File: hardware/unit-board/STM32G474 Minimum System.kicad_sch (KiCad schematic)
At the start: 19 parts, among them U4 STM32G474RET6, Y1 ECS-80-8-33Q-JES-TR

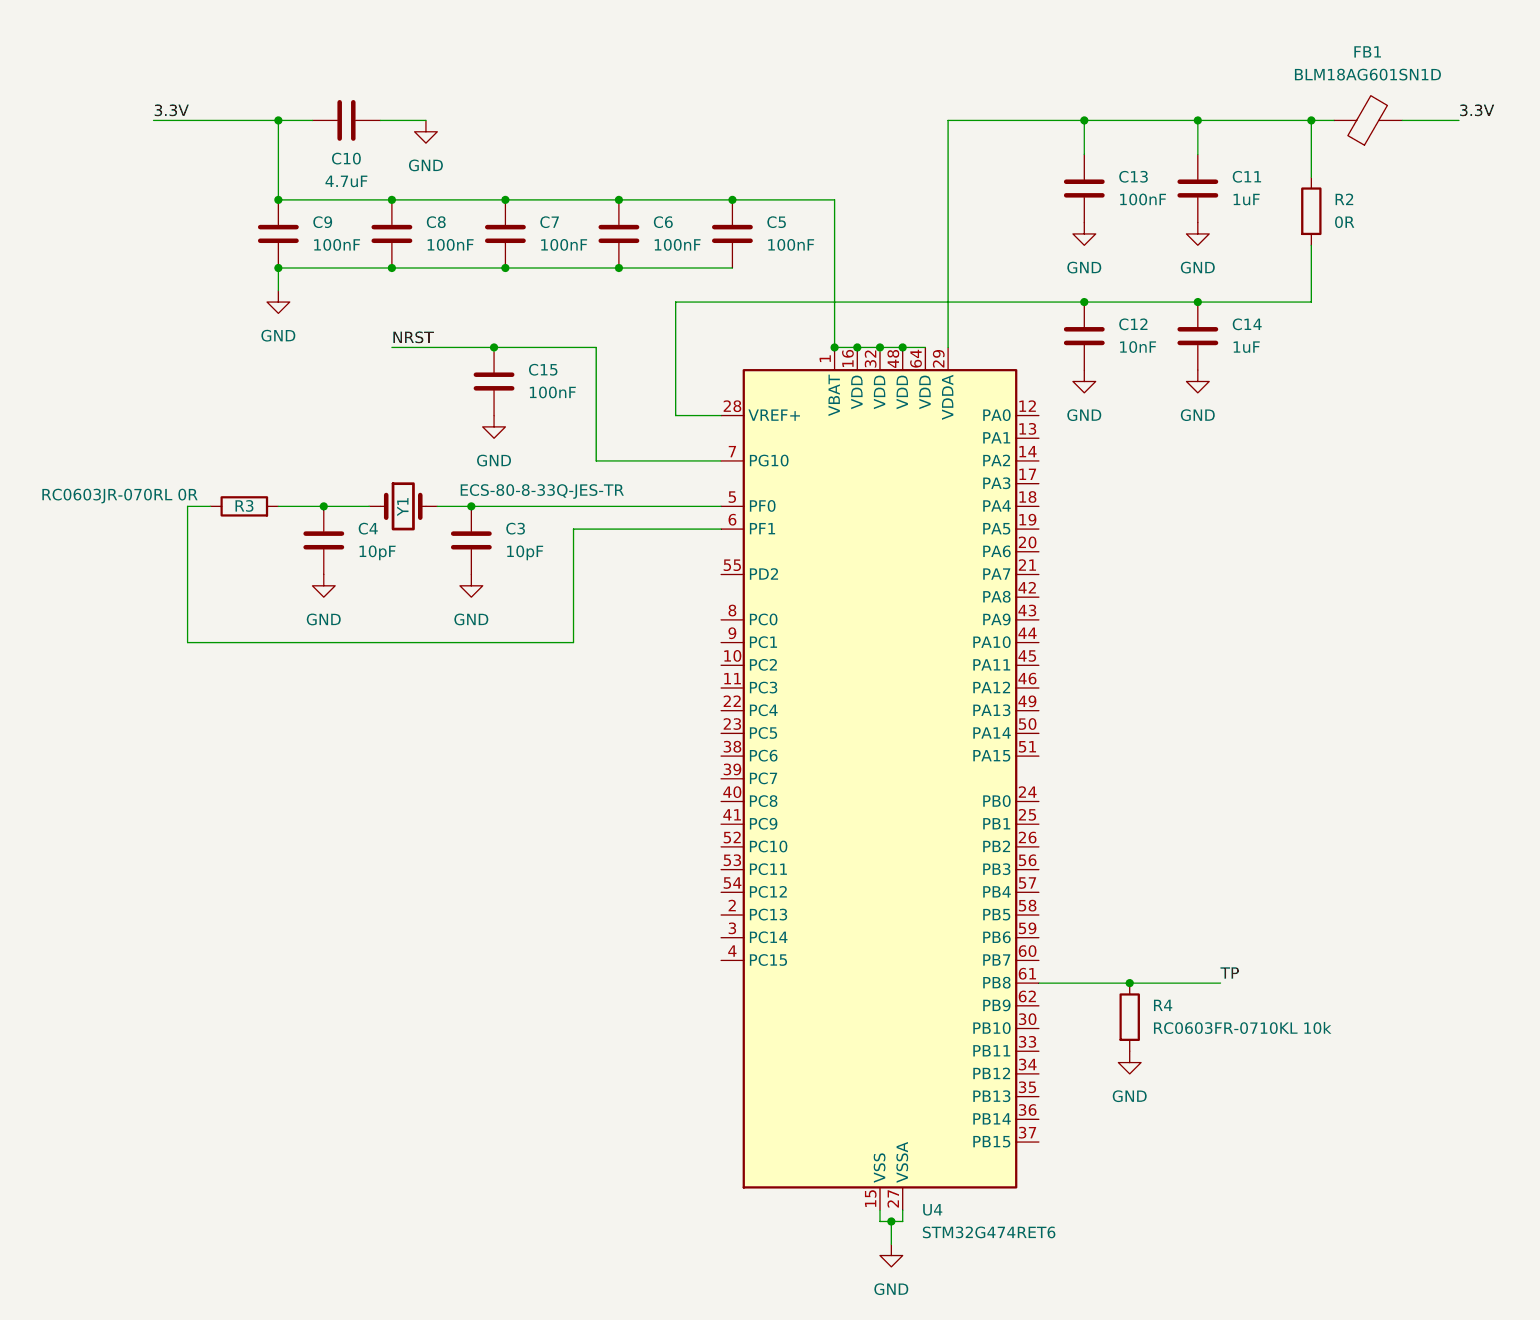
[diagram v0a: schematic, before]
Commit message: fix(hardware): resolve unit board ERC violations
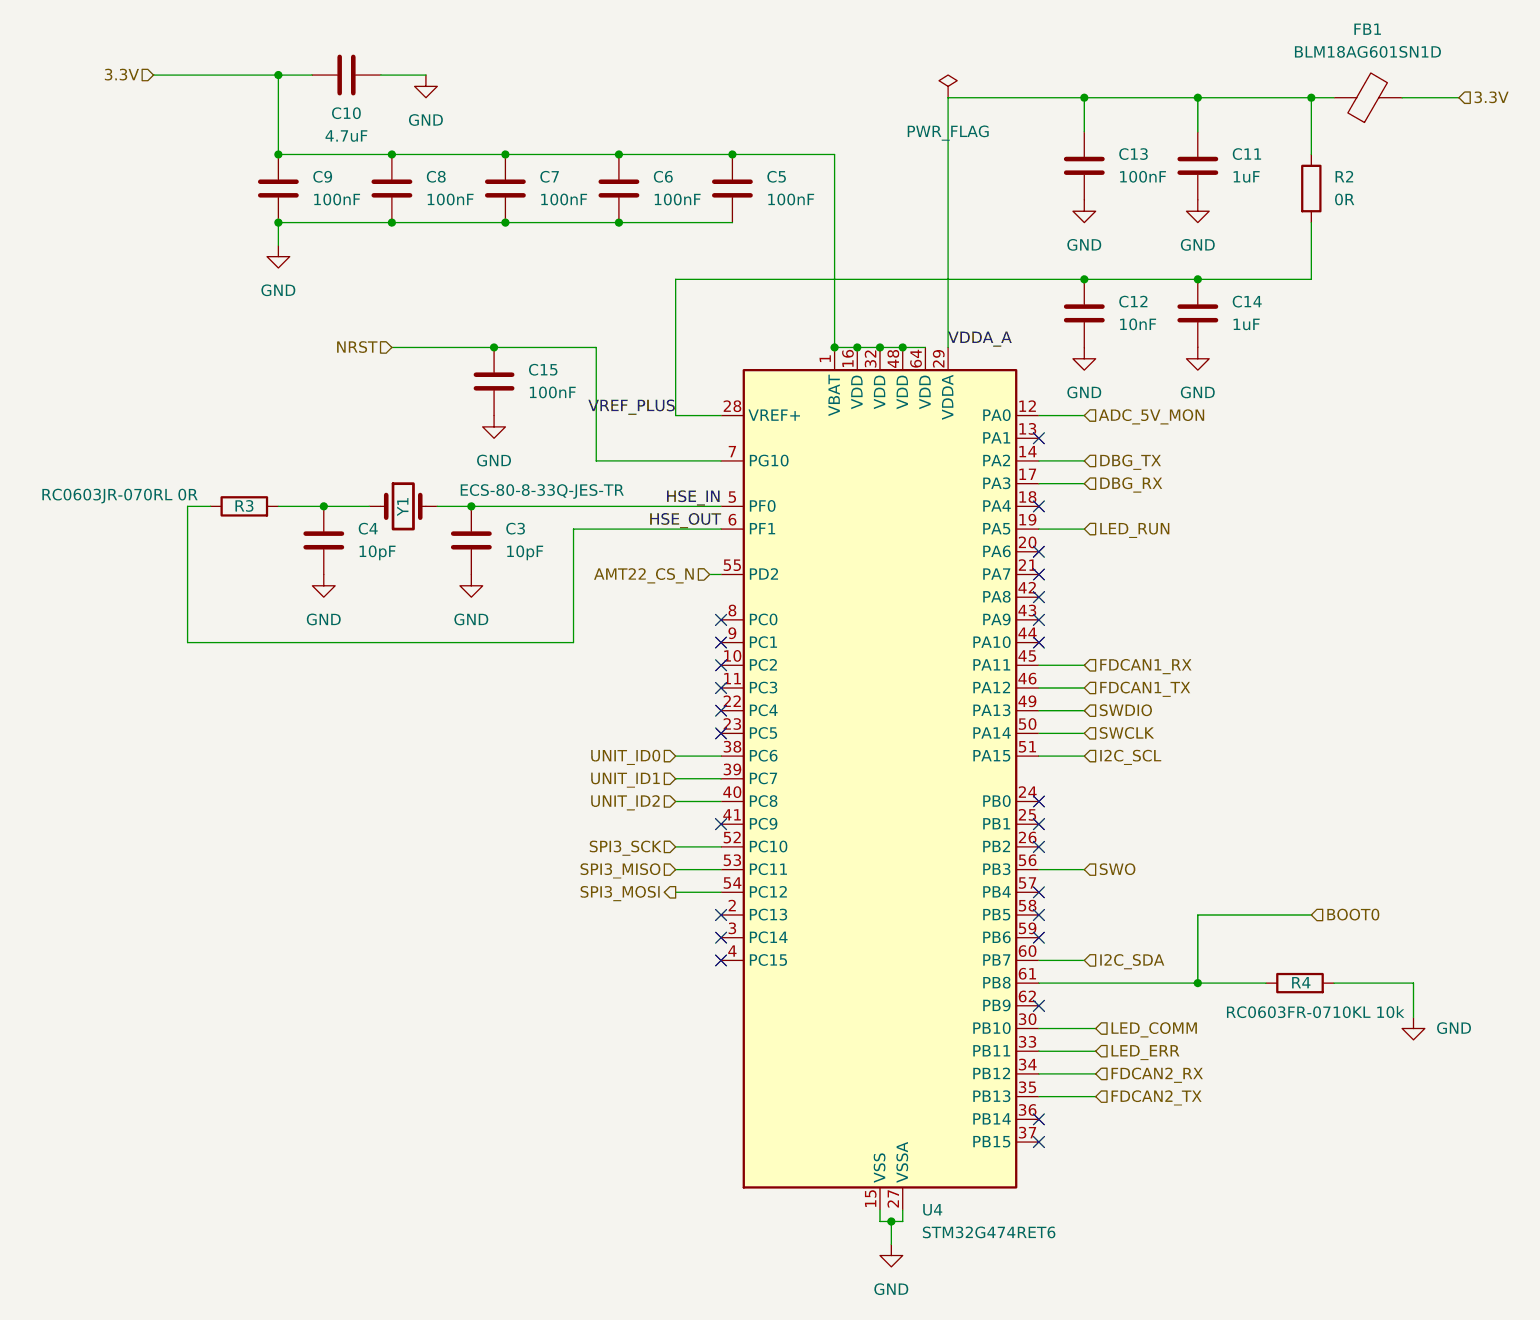
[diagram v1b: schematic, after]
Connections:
- net VDDA_A: now reaches C11.1, C13.1, FB1.1, R2.1, U4.29 (VDDA)
- net 3.3V: now reaches C10.2, C5.1, C6.1, C7.1, C8.1, C9.1, FB1.2, U4.1 (VBAT), U4.16 (VDD), U4.32 (VDD), U4.48 (VDD), U4.64 (VDD)
- net VREF_PLUS: now reaches C12.1, C14.1, R2.2, U4.28 (VREF+)
- net HSE_OUT: now reaches R3.1, U4.6 (PF1)
- net HSE_IN: now reaches C3.1, U4.5 (PF0), Y1.2
- net ADC_5V_MON: now reaches U4.12 (PA0)
- net DBG_TX: now reaches U4.14 (PA2)
- net DBG_RX: now reaches U4.17 (PA3)
- net LED_RUN: now reaches U4.19 (PA5)
- net LED_COMM: now reaches U4.30 (PB10)
- net LED_ERR: now reaches U4.33 (PB11)
- net FDCAN2_RX: now reaches U4.34 (PB12)
- net FDCAN2_TX: now reaches U4.35 (PB13)
- net UNIT_ID0: now reaches U4.38 (PC6)
- net UNIT_ID1: now reaches U4.39 (PC7)
- net UNIT_ID2: now reaches U4.40 (PC8)
- net FDCAN1_RX: now reaches U4.45 (PA11)
- net FDCAN1_TX: now reaches U4.46 (PA12)
- net SWDIO: now reaches U4.49 (PA13)
- net SWCLK: now reaches U4.50 (PA14)
- net I2C_SCL: now reaches U4.51 (PA15)
- net SPI3_SCK: now reaches U4.52 (PC10)
- net SPI3_MISO: now reaches U4.53 (PC11)
- net SPI3_MOSI: now reaches U4.54 (PC12)
- net AMT22_CS_N: now reaches U4.55 (PD2)
- net SWO: now reaches U4.56 (PB3)
- net I2C_SDA: now reaches U4.60 (PB7)
- net TP renamed BOOT0
- no-connect marks 0 -> 26
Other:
- moved on the sheet: C10, C11, C12, C13, C14, C5, C6, C7, C8, C9, FB1, R2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

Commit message: chore(hardware): update unit board design
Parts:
- removed Y1: ECS-80-8-33Q-JES-TR, Crystal:Crystal_SMD_3225-4Pin_3.2x2.5mm, symbol Device:Crystal
- added Y1: ECS-80-8-33Q-JES-TR, Crystal:Crystal_SMD_3225-4Pin_3.2x2.5mm, symbol Device:Crystal_GND24
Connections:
- net GND: now also Y1.2 (G), Y1.4 (G)
- net HSE_IN: now also Y1.3
- net at C4.1, R3.2: now also Y1.1
